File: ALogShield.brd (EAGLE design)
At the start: 53.3 x 78.5 mm, 32 parts, among them U1 DS3231MZ/V+T

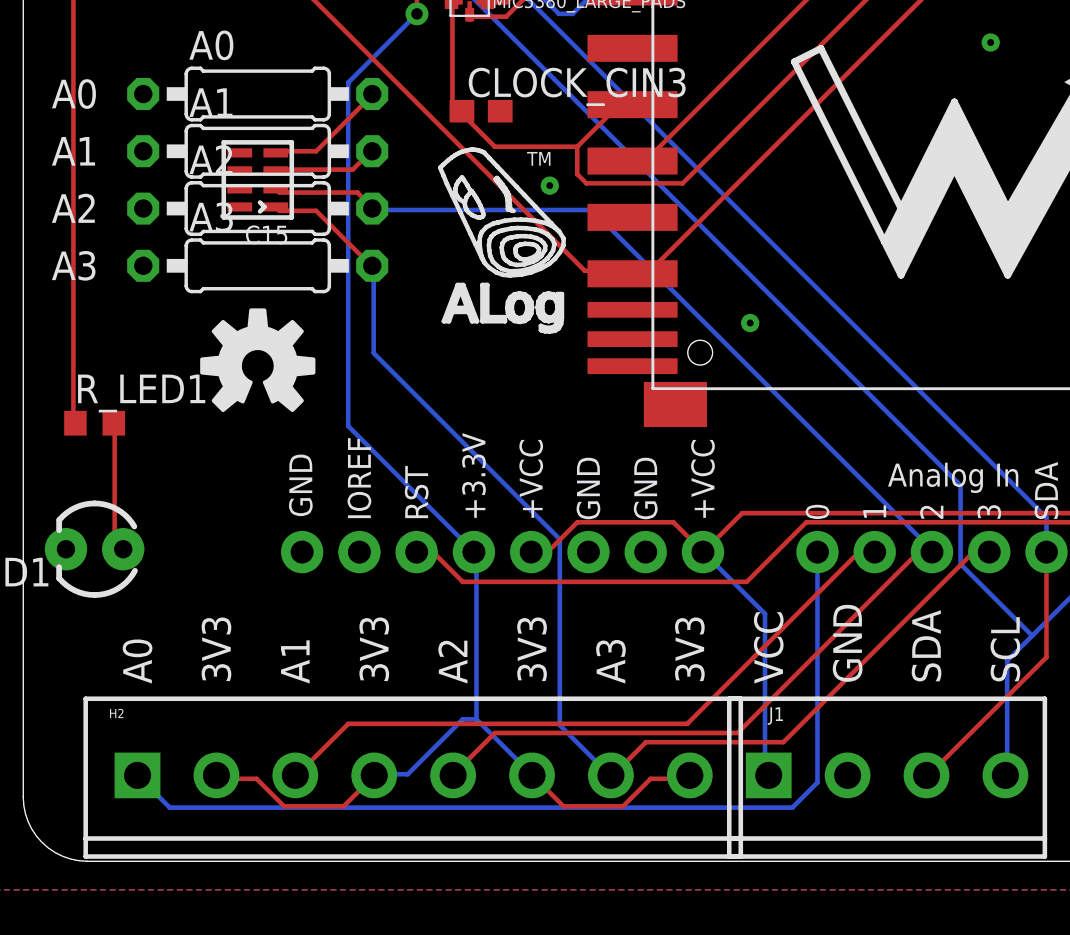
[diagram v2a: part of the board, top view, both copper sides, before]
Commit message: Reconnect Rref to analog pins
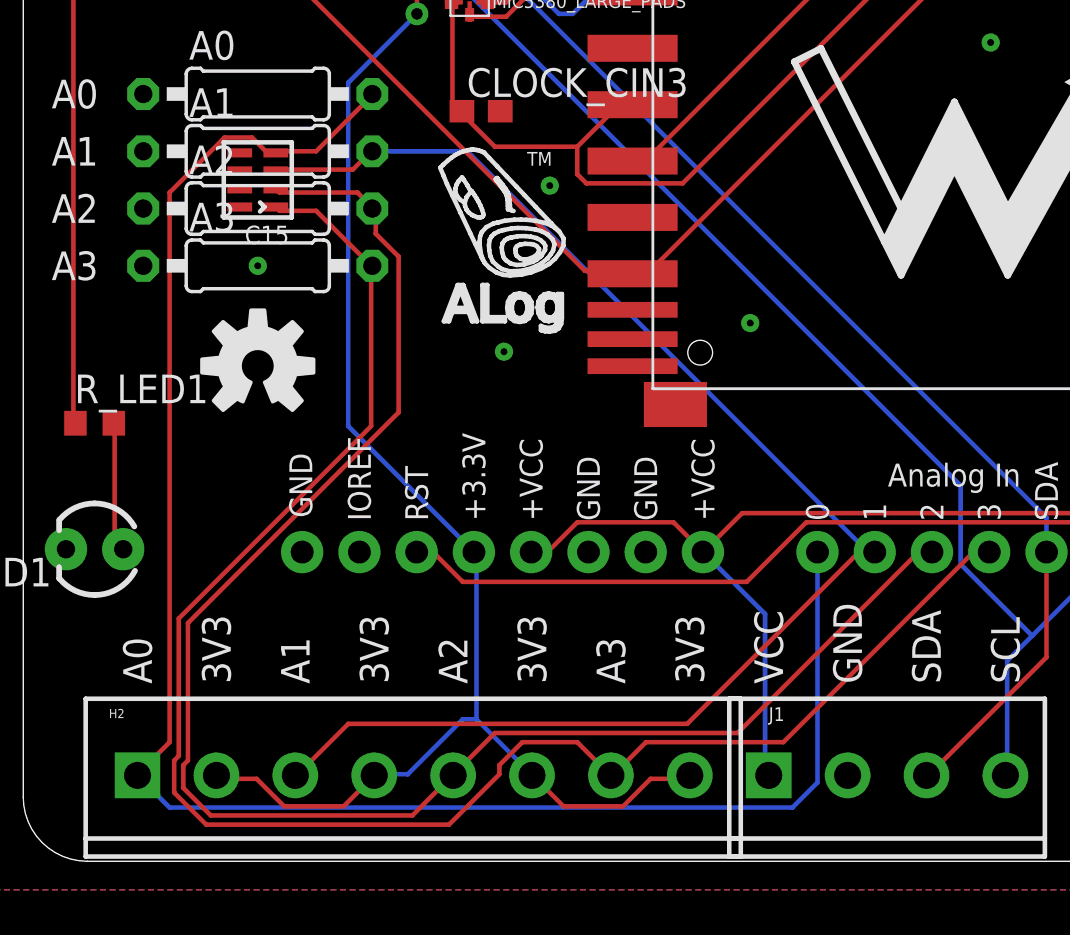
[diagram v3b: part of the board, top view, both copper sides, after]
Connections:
- removed net N$1: A0.2, C15.D1
- removed net N$2: A1.2, C15.C1
- removed net N$3: A2.2, C15.B1
- removed net N$4: A3.2, C15.A1
- net A0: now also A0.2, C15.D1
- net A1: now also A1.2, C15.C1
- net A2: now also A2.2, C15.B1
- net A3: now also A3.2, C15.A1
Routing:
- net A0: track 41.4 -> 79.3 mm
- net A1: track 29.8 -> 64.1 mm
- net A3: track 47.8 -> 75.5 mm
- net A2: track 56.5 -> 73.4 mm
- net N$1: track 5.37 -> 0.00 mm
- net N$4: track 5.36 -> 0.00 mm
- net N$3: track 4.66 -> 0.00 mm
- net N$2: track 4.63 -> 0.00 mm
- net GND: vias 16 -> 18
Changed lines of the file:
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@@
 <element name="CLOCK_BATT_DECOUP" library="rcl" package="C0603" value="0.1uF" x="22.606" y="51.943"/>
 <element name="COUT1" library="rcl" package="C0603" value="0.1uF" x="42.926" y="65.151"/>
-<element name="D2" library="semicon-smd-ipc" package="SOT23C" value="BAT54" x="42.672" y="53.594" rot="R180"/>
+<element name="D2" library="semicon-smd-ipc" package="SOT23C" value="BAT54" x="42.672" y="53.594" smashed="yes" rot="R180">
+<attribute name="NAME" x="44.577" y="51.689" size="1.27" layer="25" rot="R180"/>
+<attribute name="VALUE" x="44.577" y="56.769" size="1.27" layer="27" rot="R180"/>
+</element>
 <element name="LOG" library="SparkFun-Electromechanical" package="TACTILE-PTH" value="LOG" x="49.784" y="71.882" smashed="yes" rot="R270">
 <attribute name="PROD_ID" value=" SWCH-08441" x="-179.451" y="173.482" size="1.778" layer="27" rot="R270" display="off"/>
@@
 <attribute name="OC_FARNELL" value="unknown" x="-3.556" y="32.512" size="1.778" layer="27" display="off"/>
 </element>
-<element name="3V1" library="csandell" package="6-TMLF_SMD_PADS" value="MIC5380_LARGE_PADS" x="19.812" y="38.354"/>
+<element name="3V1" library="csandell" package="6-TMLF_SMD_PADS" value="MIC5380_LARGE_PADS" x="19.812" y="38.354" smashed="yes">
+<attribute name="NAME" x="20.812" y="38.854" size="0.6096" layer="25"/>
+<attribute name="VALUE" x="20.812" y="37.854" size="0.6096" layer="25"/>
+</element>
 <element name="C15" library="rc-master-smd" package="CECJ-CTS-031817" value="10nF" x="10.414" y="30.226" rot="R90"/>
 </elements>
@@
 <contactref element="C15" pad="B2"/>
 <contactref element="C15" pad="A2"/>
+<via x="10.414" y="26.416" extent="1-16" drill="0.3048" shape="octagon"/>
+<via x="21.336" y="22.606" extent="1-16" drill="0.3048" shape="octagon"/>
 </signal>
 <signal name="VCC">
@@
 <wire x1="40.2336" y1="13.6144" x2="40.3225" y2="13.716" width="0.2032" layer="1"/>
 <wire x1="19.1008" y1="3.8608" x2="19.08" y2="3.81" width="0.2032" layer="1"/>
-<wire x1="25.24125" y1="28.8925" x2="15.5575" y2="28.8925" width="0.2032" layer="16"/>
-<wire x1="40.3225" y1="13.81125" x2="25.24125" y2="28.8925" width="0.2032" layer="16"/>
-<wire x1="40.3225" y1="13.81125" x2="40.3225" y2="13.716" width="0.2032" layer="16"/>
+<contactref element="A2" pad="2"/>
+<contactref element="C15" pad="B1"/>
+<wire x1="14.8336" y1="29.6672" x2="11.3792" y2="29.6672" width="0.2032" layer="1"/>
+<wire x1="15.4432" y1="29.0576" x2="14.8336" y2="29.6672" width="0.2032" layer="1"/>
+<wire x1="11.3792" y1="29.6672" x2="11.214" y2="29.826" width="0.2032" layer="1"/>
+<wire x1="15.4432" y1="29.0576" x2="15.494" y2="28.956" width="0.2032" layer="1"/>
+<wire x1="15.6464" y1="27.8384" x2="15.6464" y2="28.8544" width="0.2032" layer="1"/>
+<wire x1="16.6624" y1="26.8224" x2="15.6464" y2="27.8384" width="0.2032" layer="1"/>
+<wire x1="16.6624" y1="19.9136" x2="16.6624" y2="26.8224" width="0.2032" layer="1"/>
+<wire x1="7.3152" y1="10.5664" x2="16.6624" y2="19.9136" width="0.2032" layer="1"/>
+<wire x1="7.3152" y1="4.4704" x2="7.3152" y2="10.5664" width="0.2032" layer="1"/>
+<wire x1="7.112" y1="4.2672" x2="7.3152" y2="4.4704" width="0.2032" layer="1"/>
+<wire x1="7.112" y1="3.2512" x2="7.112" y2="4.2672" width="0.2032" layer="1"/>
+<wire x1="8.3312" y1="2.032" x2="7.112" y2="3.2512" width="0.2032" layer="1"/>
+<wire x1="17.272" y1="2.032" x2="8.3312" y2="2.032" width="0.2032" layer="1"/>
+<wire x1="18.8976" y1="3.6576" x2="17.272" y2="2.032" width="0.2032" layer="1"/>
+<wire x1="15.6464" y1="28.8544" x2="15.494" y2="28.956" width="0.2032" layer="1"/>
+<wire x1="18.8976" y1="3.6576" x2="19.08" y2="3.81" width="0.2032" layer="1"/>
 </signal>
 <signal name="D3-INT1">
@@
 <wire x1="6.50875" y1="2.38125" x2="34.13125" y2="2.38125" width="0.2032" layer="16"/>
 <wire x1="5.08" y1="3.81" x2="6.50875" y2="2.38125" width="0.2032" layer="16"/>
+<contactref element="A0" pad="2"/>
+<contactref element="C15" pad="D1"/>
+<wire x1="13.0048" y1="31.496" x2="11.3792" y2="31.496" width="0.2032" layer="1"/>
+<wire x1="15.4432" y1="33.9344" x2="13.0048" y2="31.496" width="0.2032" layer="1"/>
+<wire x1="11.3792" y1="31.496" x2="11.214" y2="31.426" width="0.2032" layer="1"/>
+<wire x1="15.4432" y1="33.9344" x2="15.494" y2="34.036" width="0.2032" layer="1"/>
+<wire x1="10.7696" y1="31.496" x2="11.176" y2="31.496" width="0.2032" layer="1"/>
+<wire x1="10.16" y1="32.1056" x2="10.7696" y2="31.496" width="0.2032" layer="1"/>
+<wire x1="8.9408" y1="32.1056" x2="10.16" y2="32.1056" width="0.2032" layer="1"/>
+<wire x1="6.5024" y1="29.6672" x2="8.9408" y2="32.1056" width="0.2032" layer="1"/>
+<wire x1="6.5024" y1="5.2832" x2="6.5024" y2="29.6672" width="0.2032" layer="1"/>
+<wire x1="5.08" y1="3.8608" x2="6.5024" y2="5.2832" width="0.2032" layer="1"/>
+<wire x1="11.176" y1="31.496" x2="11.214" y2="31.426" width="0.2032" layer="1"/>
+<wire x1="5.08" y1="3.8608" x2="5.08" y2="3.81" width="0.2032" layer="1"/>
 </signal>
 <signal name="A3">
@@
 <wire x1="42.672" y1="13.6144" x2="42.8625" y2="13.716" width="0.2032" layer="1"/>
 <wire x1="26.2128" y1="3.8608" x2="26.08" y2="3.81" width="0.2032" layer="1"/>
-<wire x1="15.5575" y1="22.5425" x2="15.5575" y2="26.3525" width="0.2032" layer="16"/>
-<wire x1="23.8125" y1="14.2875" x2="15.5575" y2="22.5425" width="0.2032" layer="16"/>
-<wire x1="23.8125" y1="6.0325" x2="23.8125" y2="14.2875" width="0.2032" layer="16"/>
-<wire x1="26.035" y1="3.81" x2="23.8125" y2="6.0325" width="0.2032" layer="16"/>
-<wire x1="26.035" y1="3.81" x2="26.08" y2="3.81" width="0.2032" layer="16"/>
+<contactref element="C15" pad="A1"/>
+<contactref element="A3" pad="2"/>
+<wire x1="13.0048" y1="28.8544" x2="11.3792" y2="28.8544" width="0.2032" layer="1"/>
+<wire x1="15.4432" y1="26.416" x2="13.0048" y2="28.8544" width="0.2032" layer="1"/>
+<wire x1="11.3792" y1="28.8544" x2="11.214" y2="29.026" width="0.2032" layer="1"/>
+<wire x1="15.4432" y1="19.304" x2="15.4432" y2="26.416" width="0.2032" layer="1"/>
+<wire x1="6.9088" y1="10.7696" x2="15.4432" y2="19.304" width="0.2032" layer="1"/>
+<wire x1="6.9088" y1="4.6736" x2="6.9088" y2="10.7696" width="0.2032" layer="1"/>
+<wire x1="6.7056" y1="4.4704" x2="6.9088" y2="4.6736" width="0.2032" layer="1"/>
+<wire x1="6.7056" y1="3.048" x2="6.7056" y2="4.4704" width="0.2032" layer="1"/>
+<wire x1="8.128" y1="1.6256" x2="6.7056" y2="3.048" width="0.2032" layer="1"/>
+<wire x1="18.8976" y1="1.6256" x2="8.128" y2="1.6256" width="0.2032" layer="1"/>
+<wire x1="21.1328" y1="3.8608" x2="18.8976" y2="1.6256" width="0.2032" layer="1"/>
+<wire x1="21.1328" y1="4.2672" x2="21.1328" y2="3.8608" width="0.2032" layer="1"/>
+<wire x1="22.1488" y1="5.2832" x2="21.1328" y2="4.2672" width="0.2032" layer="1"/>
+<wire x1="24.5872" y1="5.2832" x2="22.1488" y2="5.2832" width="0.2032" layer="1"/>
+<wire x1="26.0096" y1="3.8608" x2="24.5872" y2="5.2832" width="0.2032" layer="1"/>
+<wire x1="15.4432" y1="26.416" x2="15.494" y2="26.416" width="0.2032" layer="1"/>
+<wire x1="26.0096" y1="3.8608" x2="26.08" y2="3.81" width="0.2032" layer="1"/>
 </signal>
 <signal name="D5_MANUAL_LOG">
@@
 <wire x1="37.592" y1="13.6144" x2="37.7825" y2="13.716" width="0.2032" layer="1"/>
 <wire x1="12.192" y1="3.8608" x2="12.08" y2="3.81" width="0.2032" layer="1"/>
+<contactref element="A1" pad="2"/>
+<contactref element="C15" pad="C1"/>
+<wire x1="14.6304" y1="30.6832" x2="11.3792" y2="30.6832" width="0.2032" layer="1"/>
+<wire x1="15.4432" y1="31.496" x2="14.6304" y2="30.6832" width="0.2032" layer="1"/>
+<wire x1="11.3792" y1="30.6832" x2="11.214" y2="30.626" width="0.2032" layer="1"/>
+<wire x1="15.4432" y1="31.496" x2="15.494" y2="31.496" width="0.2032" layer="1"/>
+<wire x1="19.7104" y1="31.496" x2="15.494" y2="31.496" width="0.2032" layer="16"/>
+<wire x1="37.592" y1="13.6144" x2="19.7104" y2="31.496" width="0.2032" layer="16"/>
+<wire x1="37.592" y1="13.6144" x2="37.7825" y2="13.716" width="0.2032" layer="16"/>
 </signal>
 <signal name="CS-SD">
@@
 <wire x1="23.368" y1="74.5744" x2="23.215" y2="74.676" width="0.2032" layer="1"/>
 </signal>
-<signal name="N$1">
-<contactref element="A0" pad="2"/>
-<contactref element="C15" pad="D1"/>
-<wire x1="13.0048" y1="31.496" x2="11.3792" y2="31.496" width="0.2032" layer="1"/>
-<wire x1="15.4432" y1="33.9344" x2="13.0048" y2="31.496" width="0.2032" layer="1"/>
-<wire x1="11.3792" y1="31.496" x2="11.214" y2="31.426" width="0.2032" layer="1"/>
-<wire x1="15.4432" y1="33.9344" x2="15.494" y2="34.036" width="0.2032" layer="1"/>
-</signal>
-<signal name="N$2">
-<contactref element="A1" pad="2"/>
-<contactref element="C15" pad="C1"/>
-<wire x1="14.6304" y1="30.6832" x2="11.3792" y2="30.6832" width="0.2032" layer="1"/>
-<wire x1="15.4432" y1="31.496" x2="14.6304" y2="30.6832" width="0.2032" layer="1"/>
-<wire x1="11.3792" y1="30.6832" x2="11.214" y2="30.626" width="0.2032" layer="1"/>
-<wire x1="15.4432" y1="31.496" x2="15.494" y2="31.496" width="0.2032" layer="1"/>
-</signal>
-<signal name="N$3">
-<contactref element="A2" pad="2"/>
-<contactref element="C15" pad="B1"/>
-<wire x1="14.8336" y1="29.6672" x2="11.3792" y2="29.6672" width="0.2032" layer="1"/>
-<wire x1="15.4432" y1="29.0576" x2="14.8336" y2="29.6672" width="0.2032" layer="1"/>
-<wire x1="11.3792" y1="29.6672" x2="11.214" y2="29.826" width="0.2032" layer="1"/>
-<wire x1="15.4432" y1="29.0576" x2="15.494" y2="28.956" width="0.2032" layer="1"/>
-</signal>
-<signal name="N$4">
-<contactref element="C15" pad="A1"/>
-<contactref element="A3" pad="2"/>
-<wire x1="13.0048" y1="28.8544" x2="11.3792" y2="28.8544" width="0.2032" layer="1"/>
-<wire x1="15.4432" y1="26.416" x2="13.0048" y2="28.8544" width="0.2032" layer="1"/>
-<wire x1="11.3792" y1="28.8544" x2="11.214" y2="29.026" width="0.2032" layer="1"/>
-<wire x1="15.4432" y1="26.416" x2="15.494" y2="26.416" width="0.2032" layer="1"/>
-</signal>
 </signals>

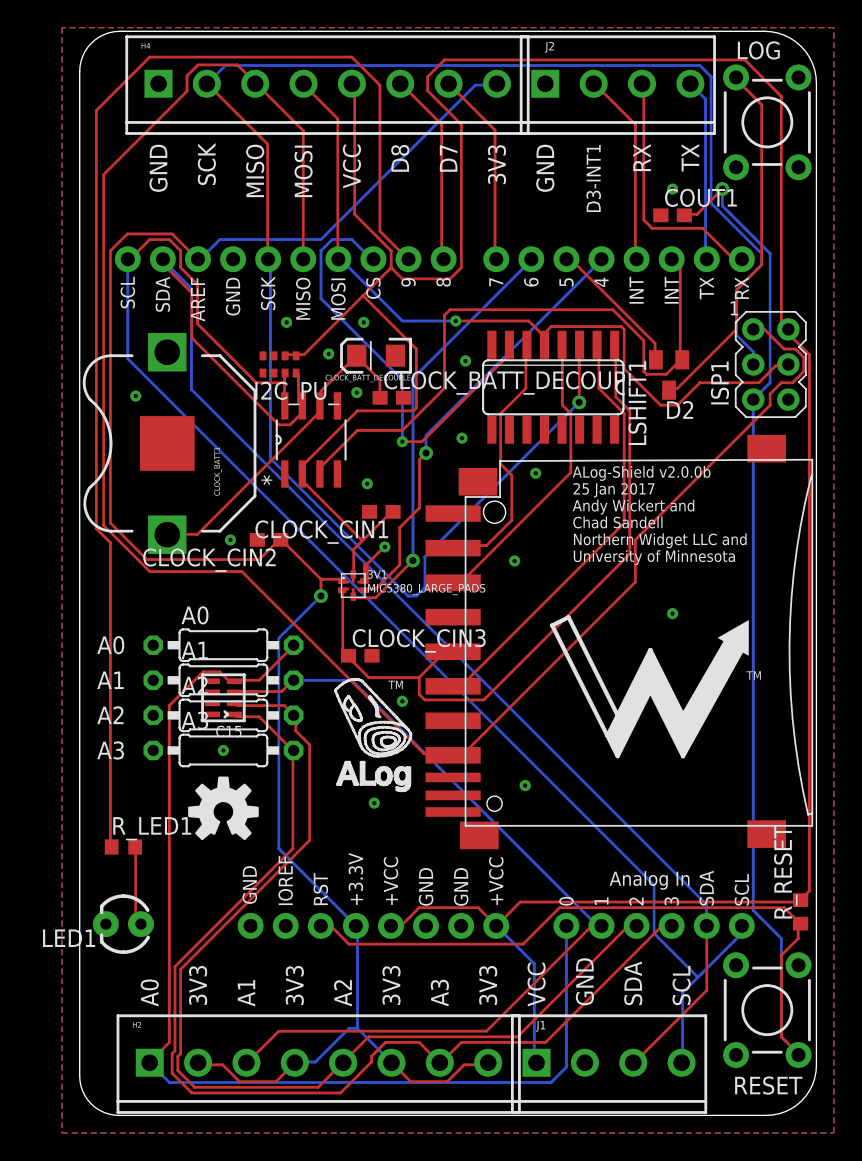
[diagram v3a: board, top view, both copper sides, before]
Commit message: Symmetry with screw terminals and buttons
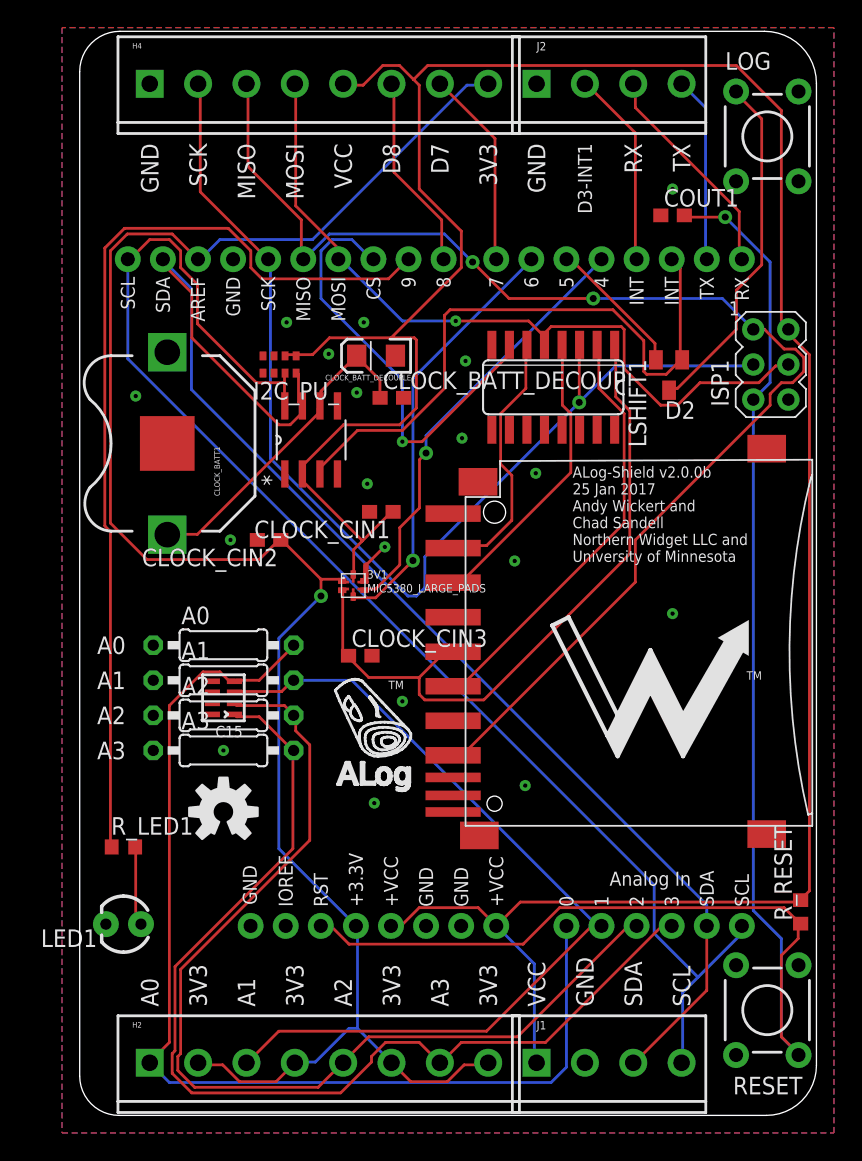
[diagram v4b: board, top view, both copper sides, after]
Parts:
- moved LOG 1.02 mm to (49.8, 70.9)
- moved J2 0.64 mm to (33.1, 74.7)
- moved H4 0.63 mm to (5.08, 74.7)
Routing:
- net CLK: track 127.9 -> 81.0 mm
- net DO: track 132.0 -> 95.3 mm, vias 0 -> 2
- net D9-LED: track 90.2 -> 69.0 mm
- net VCC: track 207.7 -> 196.1 mm
- net RESET: track 117.1 -> 114.4 mm
- net RX-I: track 18.2 -> 16.1 mm
- net N$11: track 26.5 -> 25.5 mm
- net +3V3: track 135.5 -> 134.9 mm

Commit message: Bye bye, ISP header and reset cap and R
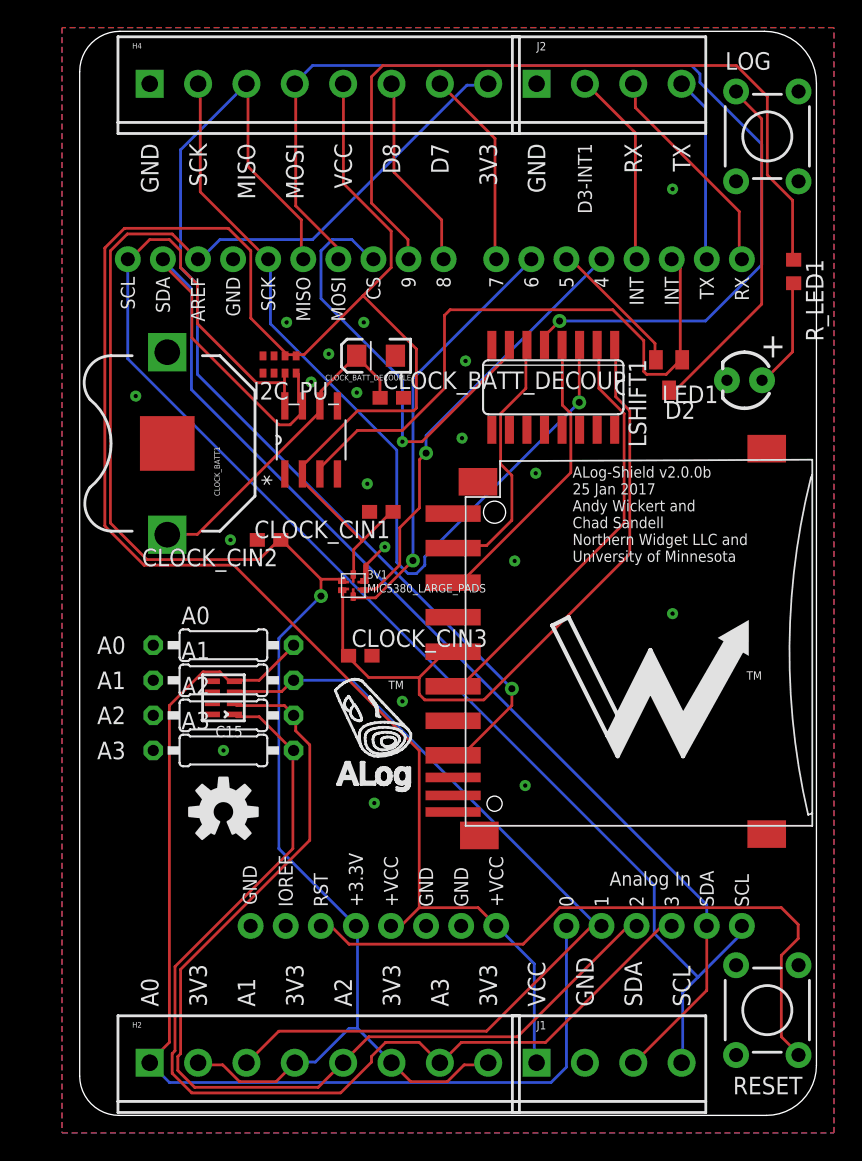
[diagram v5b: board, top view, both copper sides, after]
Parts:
- removed COUT1: 0.1uF, rcl:C0603
- removed ISP1: AVRISP-6, adafruit:AVRISP
- removed R_RESET: 10k, rcl:R0603
- moved R_LED1 63.9 mm to (51.7, 61.1), turned to 270 degrees
- moved LED1 59.8 mm to (48.1, 53.2)
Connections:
- removed net DTR: COUT1.1
- net CLK: no longer ISP1.3
- net DI: no longer ISP1.4
- net DO: no longer ISP1.1
- net GND: no longer ISP1.6
- net RESET: no longer COUT1.2, ISP1.5, R_RESET.1
- net VCC: no longer ISP1.2, R_RESET.2
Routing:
- net RESET: track 114.4 -> 47.2 mm, vias 1 -> 0
- net VCC: track 196.1 -> 159.4 mm
- net DI: track 55.9 -> 78.3 mm
- net DO: track 95.3 -> 77.1 mm, vias 2 -> 1
- net CLK: track 81.0 -> 63.9 mm
- net D9-LED: track 69.0 -> 56.9 mm
- net LED+1: track 5.75 -> 8.05 mm
- net GND: vias 18 -> 19
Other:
- board text added: "+"
